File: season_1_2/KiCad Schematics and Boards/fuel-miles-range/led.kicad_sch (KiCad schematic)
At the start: 15 parts, among them U502 TLC5957RTQ

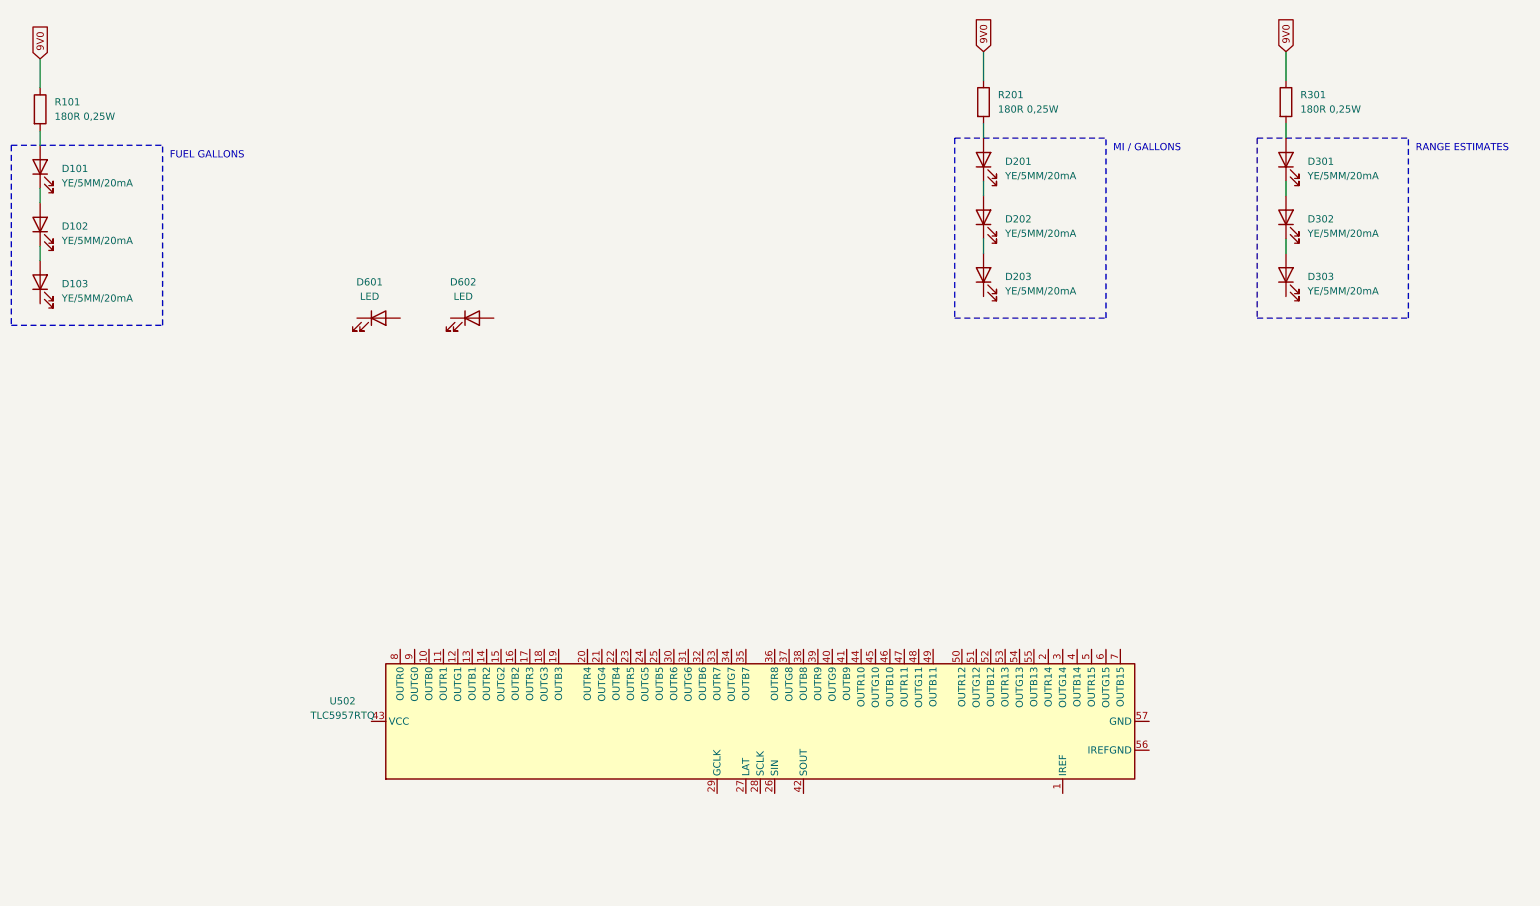
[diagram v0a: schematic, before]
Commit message: Added lots of electronic devices and routes
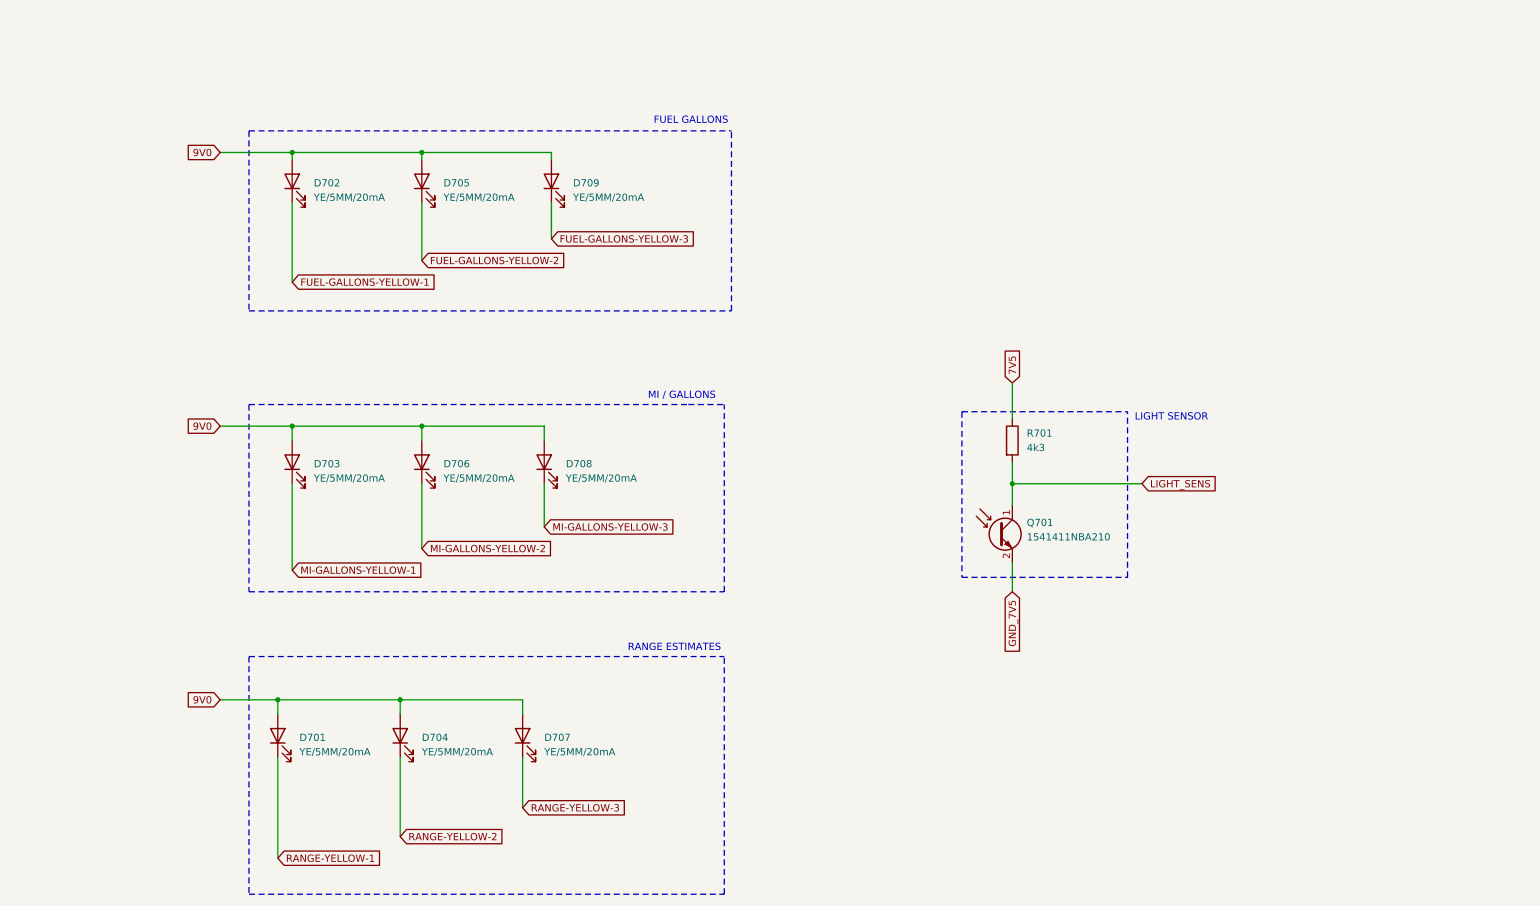
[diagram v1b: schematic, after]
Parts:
- removed D601, D602: LED, LED_THT:LED_D5.0mm, symbol Device:LED
- removed R101, R201, R301: 180R 0,25W, symbol Device:R
- removed U502: TLC5957RTQ, Package_DFN_QFN:QFN-56-1EP_8x8mm_P0.5mm_EP5.6x5.6mm_ThermalVias, symbol Driver_LED:TLC5957RTQ
- added Q701: 1541411NBA210, OptoDevice:Osram_SFH2201, symbol Sensor_Optical:BPW40
- added R701: 4k3, Resistor_SMD:R_1206_3216Metric, symbol Device:R
- D701: renamed from D301; footprint LED_THT:LED_D5.0mm -> Code99_LED:LED_5MM_YELLOW_DIFF
- D702: renamed from D101; footprint LED_THT:LED_D5.0mm -> Code99_LED:LED_5MM_YELLOW_DIFF
- D703: renamed from D201; footprint LED_THT:LED_D5.0mm -> Code99_LED:LED_5MM_YELLOW_DIFF
- D704: renamed from D302; footprint LED_THT:LED_D5.0mm -> Code99_LED:LED_5MM_YELLOW_DIFF
- D705: renamed from D102; footprint LED_THT:LED_D5.0mm -> Code99_LED:LED_5MM_YELLOW_DIFF
- D706: renamed from D202; footprint LED_THT:LED_D5.0mm -> Code99_LED:LED_5MM_YELLOW_DIFF
- D707: renamed from D303; footprint LED_THT:LED_D5.0mm -> Code99_LED:LED_5MM_YELLOW_DIFF
- D708: renamed from D203; footprint LED_THT:LED_D5.0mm -> Code99_LED:LED_5MM_YELLOW_DIFF
- D709: renamed from D103; footprint LED_THT:LED_D5.0mm -> Code99_LED:LED_5MM_YELLOW_DIFF
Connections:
- net 9V0: now also D701.2 (A), D702.2 (A), D703.2 (A), D704.2 (A), D705.2 (A), D706.2 (A), D707.2 (A), D708.2 (A), D709.2 (A)
- net FUEL-GALLONS-YELLOW-3: now reaches D709.1 (K)
- net FUEL-GALLONS-YELLOW-2: now reaches D705.1 (K)
- net FUEL-GALLONS-YELLOW-2: no longer D709.2 (A)
- net MI-GALLONS-YELLOW-2: now reaches D706.1 (K)
- net MI-GALLONS-YELLOW-2: no longer D708.2 (A)
- net MI-GALLONS-YELLOW-1: now reaches D703.1 (K)
- net MI-GALLONS-YELLOW-1: no longer D706.2 (A)
- net MI-GALLONS-YELLOW-3: now reaches D708.1 (K)
- net RANGE-YELLOW-3: now reaches D707.1 (K)
- net RANGE-YELLOW-2: now reaches D704.1 (K)
- net RANGE-YELLOW-2: no longer D707.2 (A)
- net FUEL-GALLONS-YELLOW-1: now reaches D702.1 (K)
- net FUEL-GALLONS-YELLOW-1: no longer D705.2 (A)
- net RANGE-YELLOW-1: now reaches D701.1 (K)
- net RANGE-YELLOW-1: no longer D704.2 (A)
- new net 7V5: R701.1
- new net GND_7V5: Q701.2 (E)
- new net LIGHT_SENS: Q701.1 (C), R701.2
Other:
- note added: "LIGHT SENSOR"
- moved on the sheet: D701, D702, D703, D704, D705, D706, D707, D708, D709
